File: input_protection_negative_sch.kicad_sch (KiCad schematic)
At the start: 27 parts, among them Q3 SQJQ160E, Q4 SQJQ160E, U2 LM5067

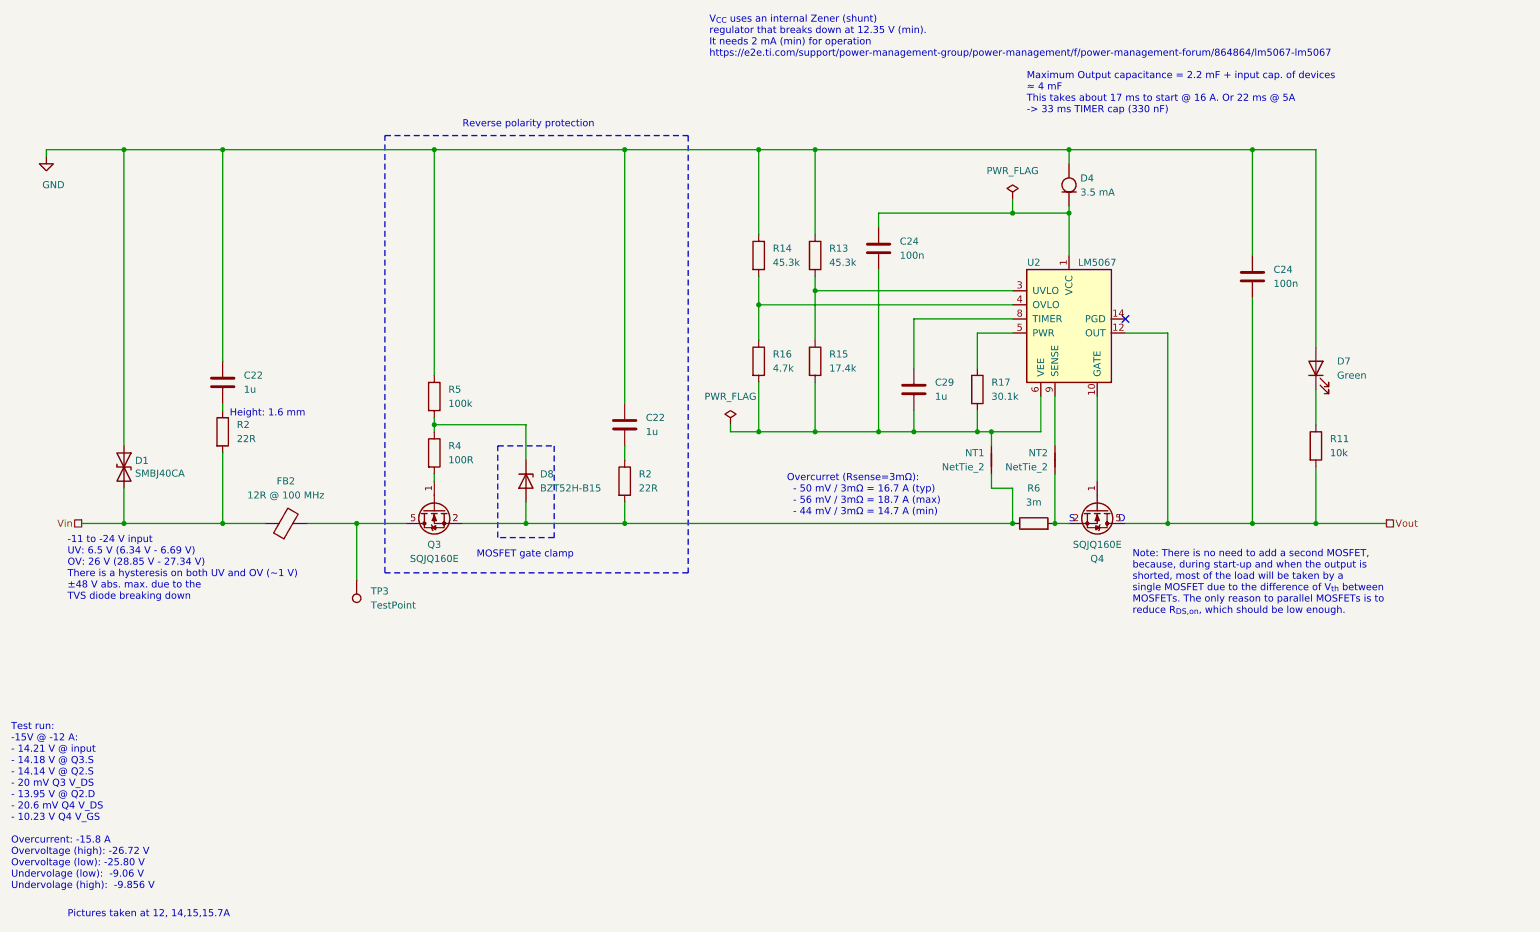
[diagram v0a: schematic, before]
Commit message: Replaced constant current diode with KiCad device available as of v7.0.10 Updated LM5067 3D model
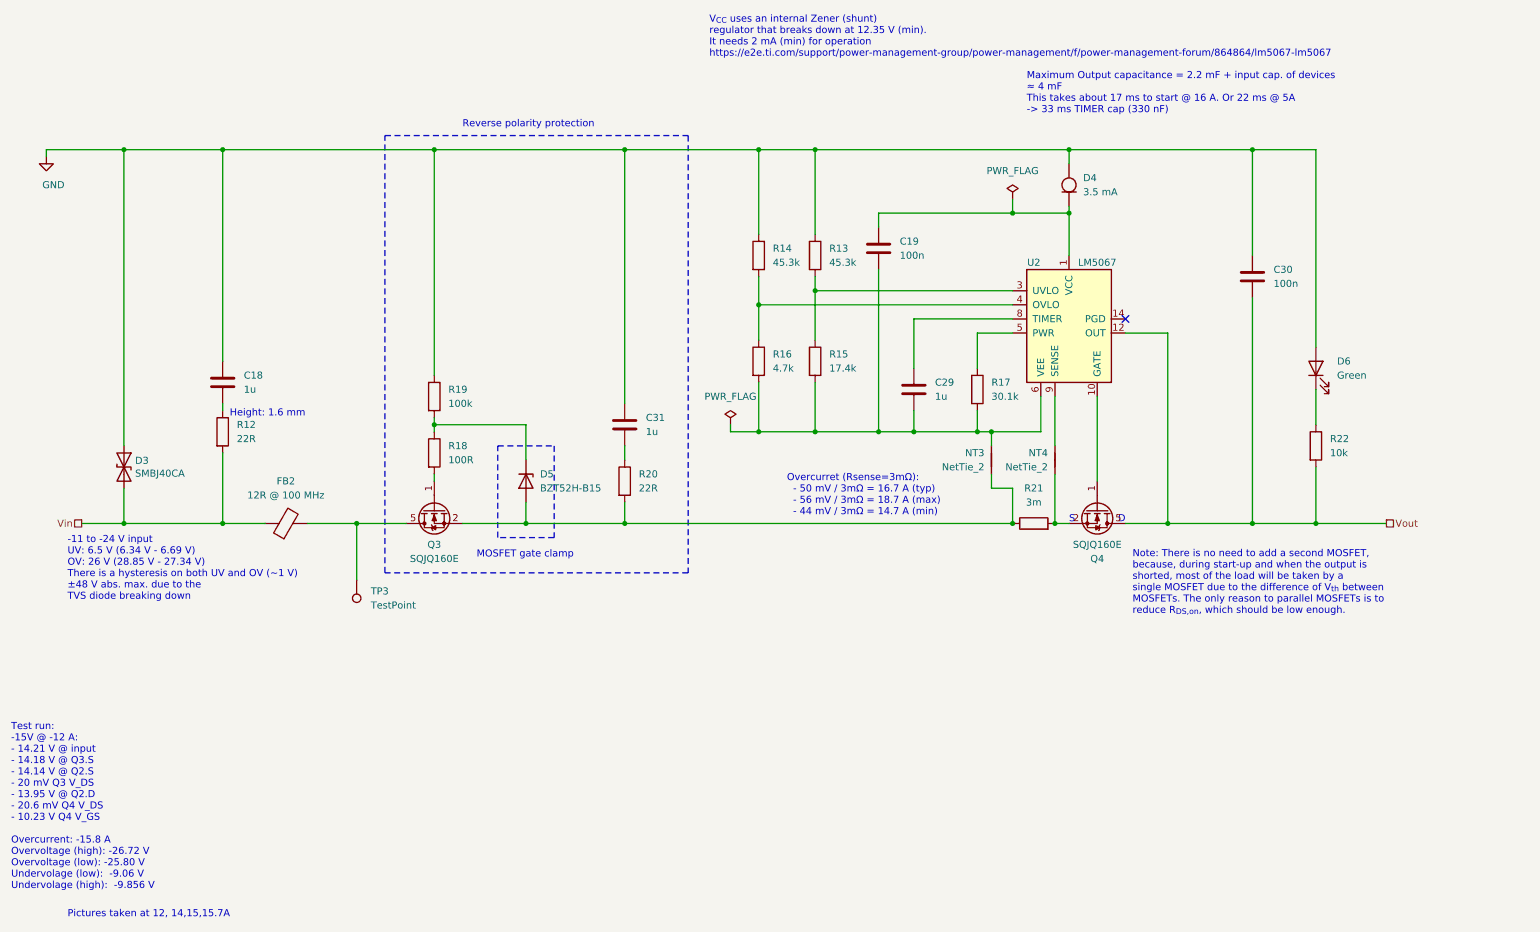
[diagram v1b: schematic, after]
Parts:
- D4: symbol constant_current_diode:D_Constant_Current -> Device:D_Constant_Current
- renumbered C22 to C18, C24 to C19, C24 to C30, C22 to C31, D1 to D3, D8 to D5, D7 to D6, NT1 to NT3, NT2 to NT4, R2 to R12, R4 to R18, R5 to R19, R2 to R20, R6 to R21, R11 to R22

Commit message: Updated power MOSFET PNs to match Mouser
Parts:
- Q3, Q4: PN SQJQ160E -> SQJQ160E-T1_GE3
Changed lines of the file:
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@@
       (effects (font (size 1.27 1.27)) hide)
     )
-    (property "PN" "SQJQ160E" (at 222.25 104.14 0)
+    (property "PN" "SQJQ160E-T1_GE3" (at 222.25 104.14 0)
       (effects (font (size 1.27 1.27)) hide)
     )
@@
       (effects (font (size 1.27 1.27)) hide)
     )
-    (property "PN" "SQJQ160E" (at 102.87 104.14 0)
-      (effects (font (size 1.27 1.27)) hide)
-    )
+    (property "PN" "SQJQ160E-T1_GE3" (at 102.87 104.14 0)
+      (effects (font (size 1.27 1.27)) hide)
+    )

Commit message: Replaced the LFPAK88 package with the new official version merged in https://gitlab.com/kicad/libraries/kicad-footprints/-/merge_requests/3408
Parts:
- Q3, Q4: footprint Custom_footprints:PowerPAK_SO-8x8L_Single_SOT-1235 -> Package_TO_SOT_SMD:LFPAK88
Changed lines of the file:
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@@
       (effects (font (size 1.27 1.27)))
     )
-    (property "Footprint" "Custom_footprints:PowerPAK_SO-8x8L_Single_SOT-1235" (at 224.79 109.22 0)
+    (property "Footprint" "Package_TO_SOT_SMD:LFPAK88" (at 224.79 109.22 0)
       (effects (font (size 1.27 1.27)) hide)
     )
@@
       (effects (font (size 1.27 1.27)))
     )
-    (property "Footprint" "Custom_footprints:PowerPAK_SO-8x8L_Single_SOT-1235" (at 100.33 109.22 0)
-      (effects (font (size 1.27 1.27)) hide)
-    )
+    (property "Footprint" "Package_TO_SOT_SMD:LFPAK88" (at 100.33 109.22 0)
+      (effects (font (size 1.27 1.27)) hide)
+    )

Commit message: Replaced Vishay SQJQ160E with official KiCad symbol
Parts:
- Q3, Q4: symbol Vishay:SQJQ160E -> Transistor_FET:SQJQ160E
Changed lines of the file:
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@@
     (effects (font (size 1.27 1.27)) (justify right))
   )
-  (symbol (lib_id "Vishay:SQJQ160E") (at 222.25 104.14 270) (unit 1)
+  (symbol (lib_id "Transistor_FET:SQJQ160E") (at 222.25 104.14 270) (unit 1)
     (in_bom yes) (on_board yes) (dnp no)
     (property "Reference" "Q4" (at 222.25 113.03 90)
@@
       (effects (font (size 1.27 1.27)))
     )
-    (property "Footprint" "Package_TO_SOT_SMD:LFPAK88" (at 224.79 109.22 0)
-      (effects (font (size 1.27 1.27)) hide)
-    )
-    (property "Datasheet" "https://www.vishay.com/docs/63059/sqjq160e.pdf" (at 222.25 104.14 0)
-      (effects (font (size 1.27 1.27)) hide)
+    (property "Footprint" "Package_TO_SOT_SMD:LFPAK88" (at 218.44 109.22 0)
+      (effects (font (size 1.27 1.27)) (justify left) hide)
+    )
+    (property "Datasheet" "https://www.vishay.com/docs/63059/sqjq160e.pdf" (at 215.9 109.22 0)
+      (effects (font (size 1.27 1.27)) (justify left) hide)
     )
     (property "MFN" "Vishay" (at 222.25 104.14 0)
@@
     (pin "1")
     (pin "2")
-    (pin "3")
     (pin "3")
     (pin "4")
@@
     )
   )
-  (symbol (lib_id "Vishay:SQJQ160E") (at 102.87 104.14 90) (mirror x) (unit 1)
+  (symbol (lib_id "Transistor_FET:SQJQ160E") (at 102.87 104.14 90) (mirror x) (unit 1)
     (in_bom yes) (on_board yes) (dnp no)
     (property "Reference" "Q3" (at 102.87 110.49 90)
@@
       (effects (font (size 1.27 1.27)))
     )
-    (property "Footprint" "Package_TO_SOT_SMD:LFPAK88" (at 100.33 109.22 0)
-      (effects (font (size 1.27 1.27)) hide)
-    )
-    (property "Datasheet" "https://www.vishay.com/docs/63059/sqjq160e.pdf" (at 102.87 104.14 0)
-      (effects (font (size 1.27 1.27)) hide)
+    (property "Footprint" "Package_TO_SOT_SMD:LFPAK88" (at 106.68 109.22 0)
+      (effects (font (size 1.27 1.27)) (justify left) hide)
+    )
+    (property "Datasheet" "https://www.vishay.com/docs/63059/sqjq160e.pdf" (at 109.22 109.22 0)
+      (effects (font (size 1.27 1.27)) (justify left) hide)
     )
     (property "MFN" "Vishay" (at 102.87 104.14 0)
@@
     (pin "1")
     (pin "2")
-    (pin "3")
     (pin "3")
     (pin "4")

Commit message: Updated layout to improve handling flexing of the PCB Changed MLCCs to flexible termination Removed thermal jumper
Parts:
- C18, C29, C31: PN C1206C105K1RACAUTO -> C1206X105K1RACAUTO; digikey# 399-13374-1-ND -> 399-13377-1-ND
- C19, C30: PN C0805C104K1RACAUTO -> C0805X104K1RACAUTO; digikey# 399-6926-1-ND -> 399-11601-1-ND
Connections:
- net Q4-S: now reaches NT4.1, Q4.2 (S), Q4.3 (S), Q4.4 (S), R21.2
- net Q3-S: now reaches D5.2 (A), NT3.1, Q3.2 (S), Q3.3 (S), Q3.4 (S), R20.2, R21.1
- net Q3-D: now reaches FB2.2, Q3.5 (D), TP3.1
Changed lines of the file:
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@@
+    (effects (font (size 1.27 1.27)) (justify left bottom))
+  )
+  (label "Q3-S" (at 109.22 106.68 0) (fields_autoplaced)
+    (effects (font (size 1.27 1.27)) (justify left bottom))
+  )
+  (label "Q3-D" (at 91.44 106.68 0) (fields_autoplaced)
+    (effects (font (size 1.27 1.27)) (justify left bottom))
+  )
+  (label "Q4-S" (at 214.63 102.87 0) (fields_autoplaced)
     (effects (font (size 1.27 1.27)) (justify left bottom))
   )
@@
       (effects (font (size 1.27 1.27)) hide)
     )
-    (property "PN" "C0805C104K1RACAUTO" (at 250.19 62.23 0)
+    (property "PN" "C0805X104K1RACAUTO" (at 250.19 62.23 0)
       (effects (font (size 1.27 1.27)) hide)
     )
@@
       (effects (font (size 1.27 1.27)) hide)
     )
-    (property "digikey#" "399-6926-1-ND" (at 250.19 62.23 0)
+    (property "digikey#" "399-11601-1-ND" (at 250.19 62.23 0)
       (effects (font (size 1.27 1.27)) hide)
     )
@@
       (effects (font (size 1.27 1.27)) hide)
     )
-    (property "PN" "C0805C104K1RACAUTO" (at 182.88 57.15 0)
+    (property "PN" "C0805X104K1RACAUTO" (at 182.88 57.15 0)
       (effects (font (size 1.27 1.27)) hide)
     )
@@
       (effects (font (size 1.27 1.27)) hide)
     )
-    (property "digikey#" "399-6926-1-ND" (at 182.88 57.15 0)
+    (property "digikey#" "399-11601-1-ND" (at 182.88 57.15 0)
       (effects (font (size 1.27 1.27)) hide)
     )
@@
       (effects (font (size 1.27 1.27)) hide)
     )
-    (property "PN" "C1206C105K1RACAUTO" (at 137.16 88.9 0)
+    (property "PN" "C1206X105K1RACAUTO" (at 137.16 88.9 0)
       (effects (font (size 1.27 1.27)) hide)
     )
@@
       (effects (font (size 1.27 1.27)) hide)
     )
-    (property "digikey#" "399-13374-1-ND" (at 137.16 88.9 0)
+    (property "digikey#" "399-13377-1-ND" (at 137.16 88.9 0)
       (effects (font (size 1.27 1.27)) hide)
     )
@@
       (effects (font (size 1.27 1.27)) hide)
     )
-    (property "PN" "C1206C105K1RACAUTO" (at 64.77 81.28 0)
+    (property "PN" "C1206X105K1RACAUTO" (at 64.77 81.28 0)
       (effects (font (size 1.27 1.27)) hide)
     )
@@
       (effects (font (size 1.27 1.27)) hide)
     )
-    (property "digikey#" "399-13374-1-ND" (at 64.77 81.28 0)
+    (property "digikey#" "399-13377-1-ND" (at 64.77 81.28 0)
       (effects (font (size 1.27 1.27)) hide)
     )
@@
       (effects (font (size 1.27 1.27)) hide)
     )
-    (property "PN" "C1206C105K1RACAUTO" (at 189.23 82.55 0)
+    (property "PN" "C1206X105K1RACAUTO" (at 189.23 82.55 0)
       (effects (font (size 1.27 1.27)) hide)
     )
@@
       (effects (font (size 1.27 1.27)) hide)
     )
-    (property "digikey#" "399-13374-1-ND" (at 189.23 82.55 0)
-      (effects (font (size 1.27 1.27)) hide)
-    )
+    (property "digikey#" "399-13377-1-ND" (at 189.23 82.55 0)
+      (effects (font (size 1.27 1.27)) hide)
+    )
